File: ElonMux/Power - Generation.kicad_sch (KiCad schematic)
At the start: 34 parts, among them IC601 LTC3126IUFD#PBF

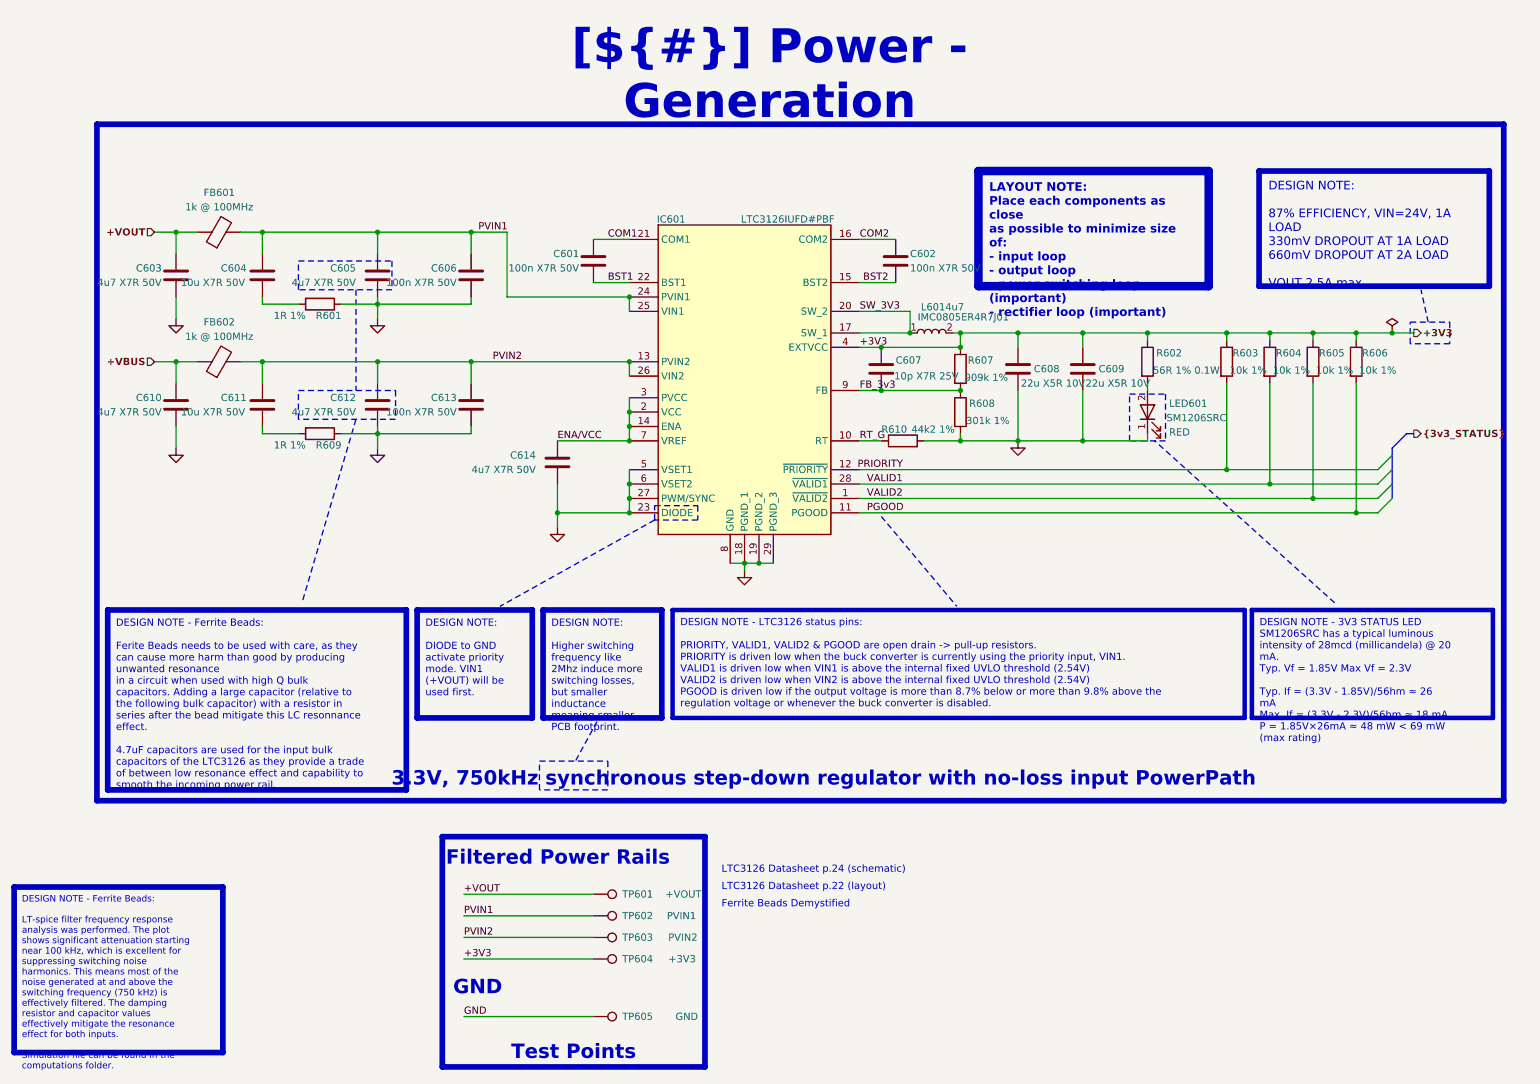
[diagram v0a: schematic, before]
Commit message: Done with changes of v1.1, need to final check and order
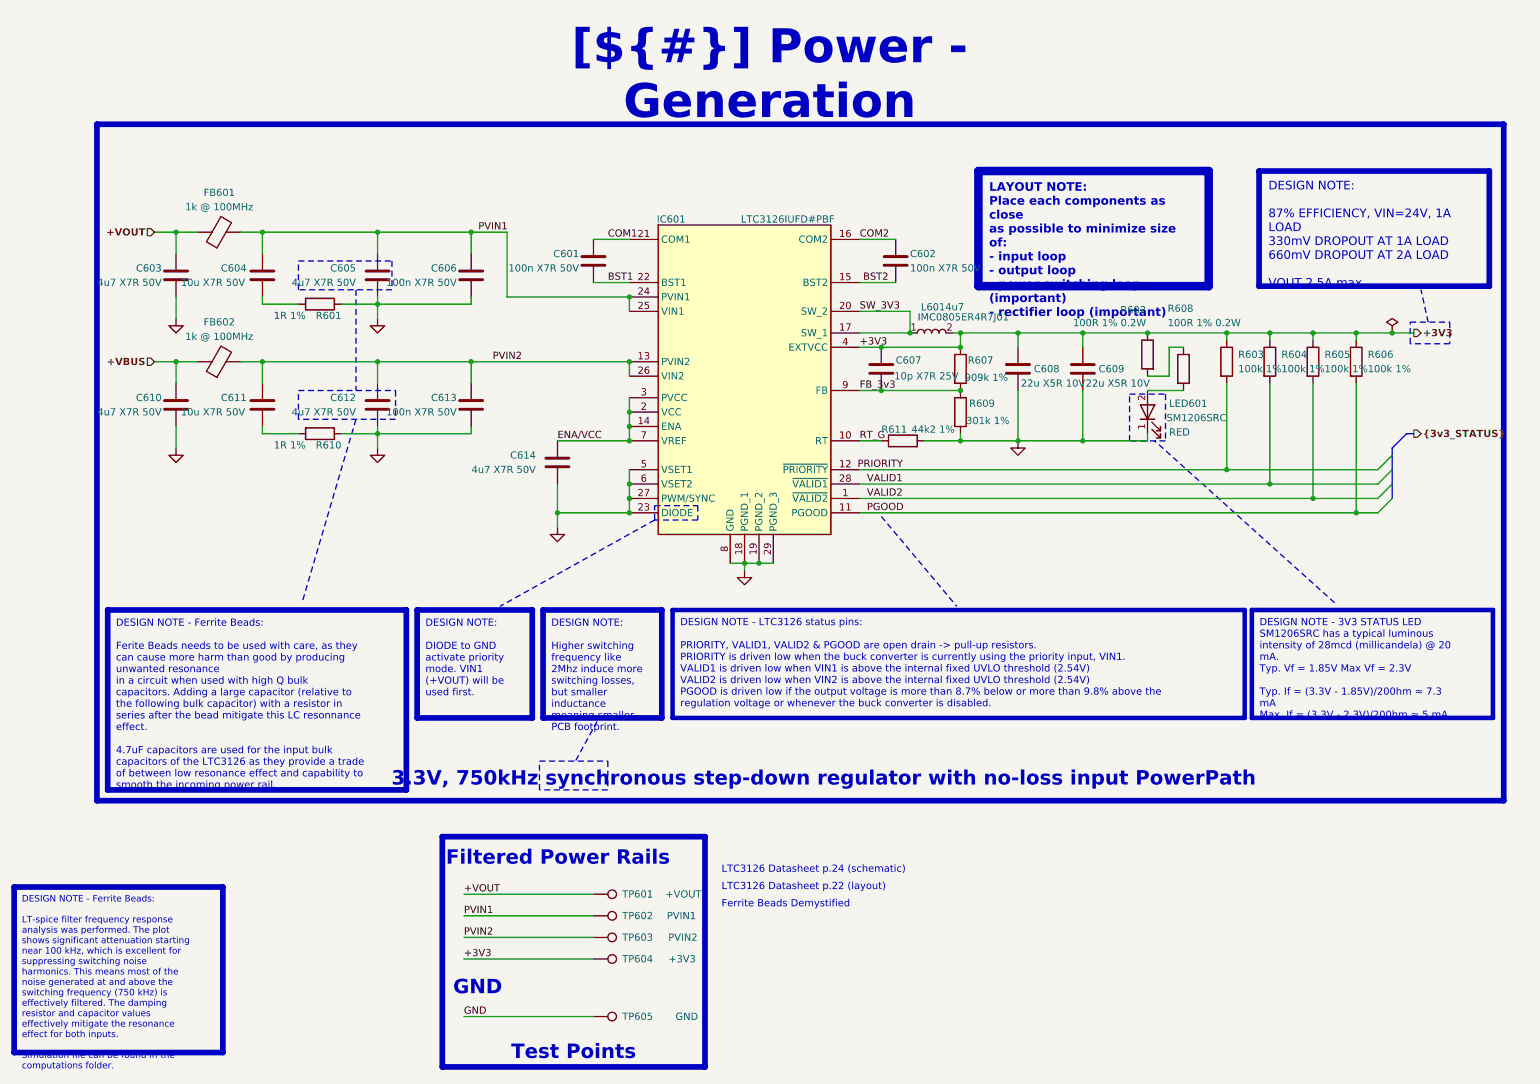
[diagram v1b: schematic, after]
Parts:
- added R608: 100R 1% 0.2W, Resistor_SMD:R_0402_1005Metric, symbol Device:R
- R602: value 56R 1% 0.1W -> 100R 1% 0.2W; Manufacturer Panasonic -> Vishay / Dale; Manufacturer Part Number ERJ-2RKF56R0X -> CRCW0402100RFKEDHP; Supplier Part Number 667-ERJ-2RKF56R0X -> 71-CRCW0402100RFKEDH
- R603, R604, R605, R606: value 10k 1% -> 100k 1%; Manufacturer KOA Speer -> Panasonic; Manufacturer Part Number SG73P1EWTTP1002F -> ERJ-2RKF1003X; Supplier Part Number 660-SG73P1EWTTP1002F -> 667-ERJ-2RKF1003X
- renumbered R608 to R609, R609 to R610, R610 to R611
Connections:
- net at R602.2: now also R608.1; no longer LED601.2 (A)
- new net: LED601.2 (A), R608.2
